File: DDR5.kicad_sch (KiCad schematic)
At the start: 2 parts, among them U12 DDR504111002KQ

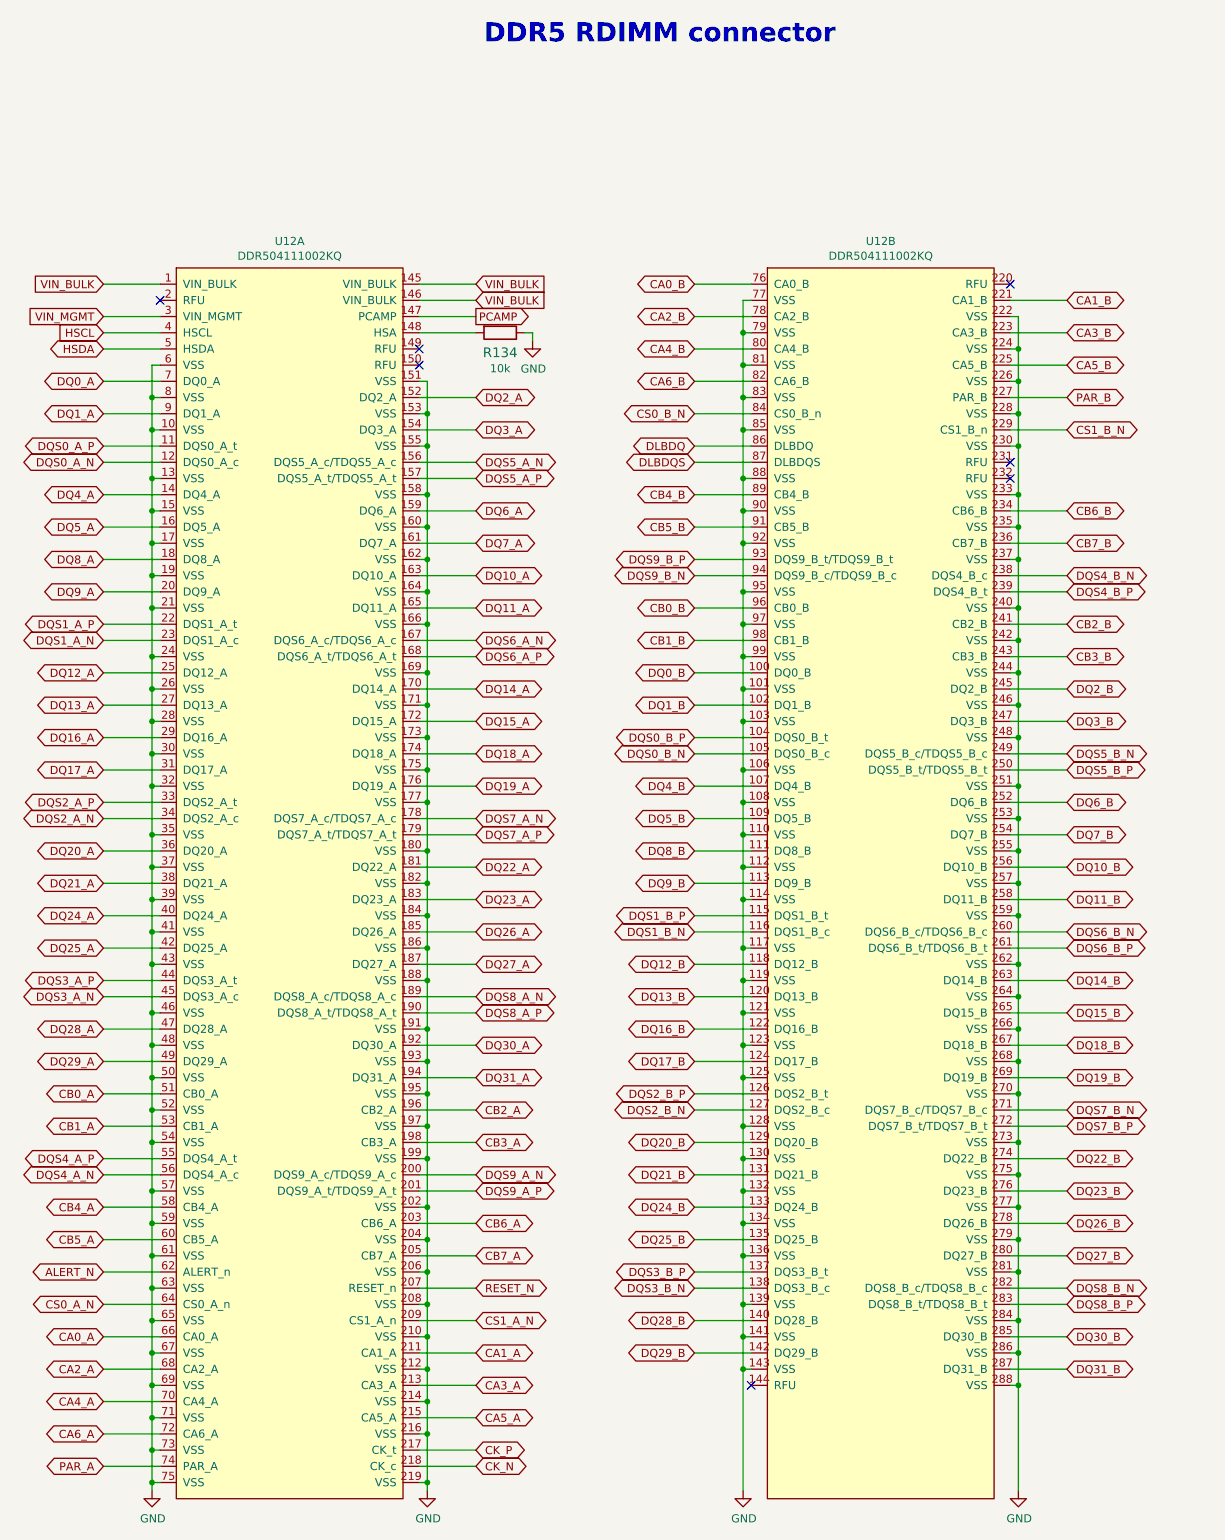
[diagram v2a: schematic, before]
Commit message: Introduce component standarization
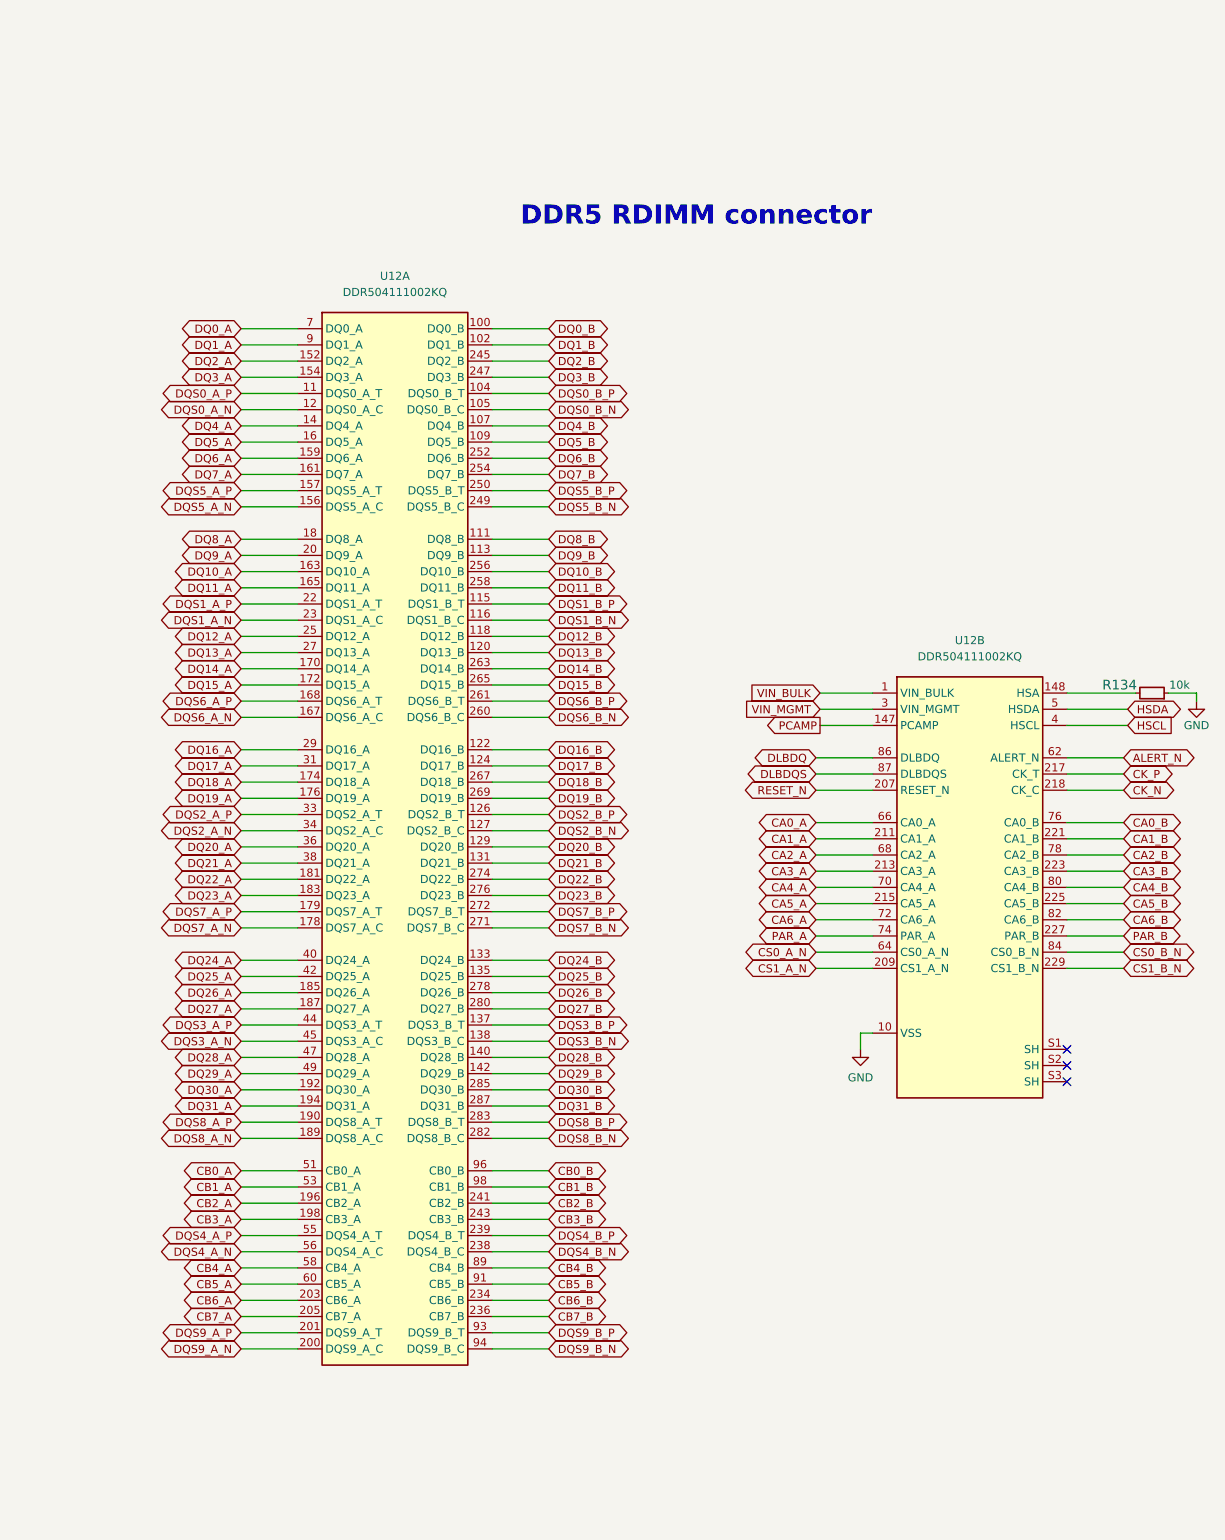
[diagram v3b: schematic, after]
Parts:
- R134: footprint data-center-rdimm-ddr5-tester-footprints:0402-res -> data-center-rdimm-ddr5-tester-footprints:R_0402_1005Metric; Author (none) -> Antmicro; License (none) -> Apache-2.0; MPN CRCW040210K0FKEDHP -> CR0402-FX-1002GLF; Manufacturer VISHAY -> Bourns; Tolerance (none) -> 1%
- U12: value DDR504111002KQ -> Bus_DDR5_DDR504111002KQ; footprint data-center-rdimm-ddr5-tester-footprints:DDR504111002KQ -> data-center-rdimm-ddr5-tester-footprints:Bus_DDR5_Socket_Amphenol_DDR504111002KQ; symbol data-center-rdimm-ddr5-tester:DDR504111002KQ -> data-center-rdimm-ddr5-tester:Bus_DDR5_DDR504111002KQ; Author (none) -> Antmicro; License (none) -> Apache-2.0; Manufacturer (none) -> Amphenol; Manufaturer Amphenol FCI -> (none)
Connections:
- net ALERT_N: now also U12.62 (ALERT_N); no longer U12.62 (ALERT_n)
- net CA0_A: now also U12.66 (CA0_A); no longer U12.66 (CA0_A)
- net CA1_A: now also U12.211 (CA1_A); no longer U12.211 (CA1_A)
- net CA2_A: now also U12.68 (CA2_A); no longer U12.68 (CA2_A)
- net CA3_A: now also U12.213 (CA3_A); no longer U12.213 (CA3_A)
- net CA4_A: now also U12.70 (CA4_A); no longer U12.70 (CA4_A)
- net CA5_A: now also U12.215 (CA5_A); no longer U12.215 (CA5_A)
- net CA6_A: now also U12.72 (CA6_A); no longer U12.72 (CA6_A)
- net CB0_B: now also U12.96 (CB0_B); no longer U12.96 (CB0_B)
- net CB1_B: now also U12.98 (CB1_B); no longer U12.98 (CB1_B)
- net CB2_B: now also U12.241 (CB2_B); no longer U12.241 (CB2_B)
- net CB3_B: now also U12.243 (CB3_B); no longer U12.243 (CB3_B)
- net CB4_B: now also U12.89 (CB4_B); no longer U12.89 (CB4_B)
- net CB5_B: now also U12.91 (CB5_B); no longer U12.91 (CB5_B)
- net CB6_B: now also U12.234 (CB6_B); no longer U12.234 (CB6_B)
- net CB7_B: now also U12.236 (CB7_B); no longer U12.236 (CB7_B)
- net CK_N: now also U12.218 (CK_C); no longer U12.218 (CK_c)
- net CK_P: now also U12.217 (CK_T); no longer U12.217 (CK_t)
- net CS0_A_N: now also U12.64 (CS0_A_N); no longer U12.64 (CS0_A_n)
- net CS1_A_N: now also U12.209 (CS1_A_N); no longer U12.209 (CS1_A_n)
- net DQ0_B: now also U12.100 (DQ0_B); no longer U12.100 (DQ0_B)
- net DQ10_B: now also U12.256 (DQ10_B); no longer U12.256 (DQ10_B)
- net DQ11_B: now also U12.258 (DQ11_B); no longer U12.258 (DQ11_B)
- net DQ12_B: now also U12.118 (DQ12_B); no longer U12.118 (DQ12_B)
- net DQ13_B: now also U12.120 (DQ13_B); no longer U12.120 (DQ13_B)
- net DQ14_B: now also U12.263 (DQ14_B); no longer U12.263 (DQ14_B)
- net DQ15_B: now also U12.265 (DQ15_B); no longer U12.265 (DQ15_B)
- net DQ16_B: now also U12.122 (DQ16_B); no longer U12.122 (DQ16_B)
- net DQ17_B: now also U12.124 (DQ17_B); no longer U12.124 (DQ17_B)
- net DQ18_B: now also U12.267 (DQ18_B); no longer U12.267 (DQ18_B)
- net DQ19_B: now also U12.269 (DQ19_B); no longer U12.269 (DQ19_B)
- net DQ1_B: now also U12.102 (DQ1_B); no longer U12.102 (DQ1_B)
- net DQ20_B: now also U12.129 (DQ20_B); no longer U12.129 (DQ20_B)
- net DQ21_B: now also U12.131 (DQ21_B); no longer U12.131 (DQ21_B)
- net DQ22_B: now also U12.274 (DQ22_B); no longer U12.274 (DQ22_B)
- net DQ23_B: now also U12.276 (DQ23_B); no longer U12.276 (DQ23_B)
- net DQ24_B: now also U12.133 (DQ24_B); no longer U12.133 (DQ24_B)
- net DQ25_B: now also U12.135 (DQ25_B); no longer U12.135 (DQ25_B)
- net DQ26_B: now also U12.278 (DQ26_B); no longer U12.278 (DQ26_B)
- net DQ27_B: now also U12.280 (DQ27_B); no longer U12.280 (DQ27_B)
- net DQ28_B: now also U12.140 (DQ28_B); no longer U12.140 (DQ28_B)
- net DQ29_B: now also U12.142 (DQ29_B); no longer U12.142 (DQ29_B)
- net DQ2_B: now also U12.245 (DQ2_B); no longer U12.245 (DQ2_B)
- net DQ30_B: now also U12.285 (DQ30_B); no longer U12.285 (DQ30_B)
- net DQ31_B: now also U12.287 (DQ31_B); no longer U12.287 (DQ31_B)
- net DQ3_B: now also U12.247 (DQ3_B); no longer U12.247 (DQ3_B)
- net DQ4_B: now also U12.107 (DQ4_B); no longer U12.107 (DQ4_B)
- net DQ5_B: now also U12.109 (DQ5_B); no longer U12.109 (DQ5_B)
- net DQ6_B: now also U12.252 (DQ6_B); no longer U12.252 (DQ6_B)
- net DQ7_B: now also U12.254 (DQ7_B); no longer U12.254 (DQ7_B)
- net DQ8_B: now also U12.111 (DQ8_B); no longer U12.111 (DQ8_B)
- net DQ9_B: now also U12.113 (DQ9_B); no longer U12.113 (DQ9_B)
- net DQS0_B_N: now also U12.105 (DQS0_B_C); no longer U12.105 (DQS0_B_c)
- net DQS0_B_P: now also U12.104 (DQS0_B_T); no longer U12.104 (DQS0_B_t)
- net DQS1_B_N: now also U12.116 (DQS1_B_C); no longer U12.116 (DQS1_B_c)
- net DQS1_B_P: now also U12.115 (DQS1_B_T); no longer U12.115 (DQS1_B_t)
- net DQS2_B_N: now also U12.127 (DQS2_B_C); no longer U12.127 (DQS2_B_c)
- net DQS2_B_P: now also U12.126 (DQS2_B_T); no longer U12.126 (DQS2_B_t)
- net DQS3_B_N: now also U12.138 (DQS3_B_C); no longer U12.138 (DQS3_B_c)
- net DQS3_B_P: now also U12.137 (DQS3_B_T); no longer U12.137 (DQS3_B_t)
- net DQS4_B_N: now also U12.238 (DQS4_B_C); no longer U12.238 (DQS4_B_c)
- net DQS4_B_P: now also U12.239 (DQS4_B_T); no longer U12.239 (DQS4_B_t)
- net DQS5_B_N: now also U12.249 (DQS5_B_C); no longer U12.249 (DQS5_B_c/TDQS5_B_c)
- net DQS5_B_P: now also U12.250 (DQS5_B_T); no longer U12.250 (DQS5_B_t/TDQS5_B_t)
- net DQS6_B_N: now also U12.260 (DQS6_B_C); no longer U12.260 (DQS6_B_c/TDQS6_B_c)
- net DQS6_B_P: now also U12.261 (DQS6_B_T); no longer U12.261 (DQS6_B_t/TDQS6_B_t)
- net DQS7_B_N: now also U12.271 (DQS7_B_C); no longer U12.271 (DQS7_B_c/TDQS7_B_c)
- net DQS7_B_P: now also U12.272 (DQS7_B_T); no longer U12.272 (DQS7_B_t/TDQS7_B_t)
- net DQS8_B_N: now also U12.282 (DQS8_B_C); no longer U12.282 (DQS8_B_c/TDQS8_B_c)
- net DQS8_B_P: now also U12.283 (DQS8_B_T); no longer U12.283 (DQS8_B_t/TDQS8_B_t)
- net DQS9_B_N: now also U12.94 (DQS9_B_C); no longer U12.94 (DQS9_B_c/TDQS9_B_c)
- net DQS9_B_P: now also U12.93 (DQS9_B_T); no longer U12.93 (DQS9_B_t/TDQS9_B_t)
- net GND: now also U12.10 (VSS), U12.13 (VSS), U12.15 (VSS), U12.151 (VSS), U12.153 (VSS), U12.155 (VSS), U12.158 (VSS), U12.160 (VSS), U12.162 (VSS), U12.164 (VSS), U12.166 (VSS), U12.169 (VSS), U12.17 (VSS), U12.171 (VSS), U12.173 (VSS), U12.175 (VSS), U12.177 (VSS), U12.180 (VSS), U12.182 (VSS), U12.184 (VSS), U12.186 (VSS), U12.188 (VSS), U12.19 (VSS), U12.191 (VSS), U12.193 (VSS), U12.195 (VSS), U12.197 (VSS), U12.199 (VSS), U12.202 (VSS), U12.204 (VSS), U12.206 (VSS), U12.208 (VSS), U12.21 (VSS), U12.210 (VSS), U12.212 (VSS), U12.214 (VSS), U12.216 (VSS), U12.219 (VSS), U12.24 (VSS), U12.26 (VSS), U12.28 (VSS), U12.30 (VSS), U12.32 (VSS), U12.35 (VSS), U12.37 (VSS), U12.39 (VSS), U12.41 (VSS), U12.43 (VSS), U12.46 (VSS), U12.48 (VSS), U12.50 (VSS), U12.52 (VSS), U12.54 (VSS), U12.57 (VSS), U12.59 (VSS), U12.6 (VSS), U12.61 (VSS), U12.63 (VSS), U12.65 (VSS), U12.67 (VSS), U12.69 (VSS), U12.71 (VSS), U12.73 (VSS), U12.75 (VSS), U12.8 (VSS); no longer U12.10 (VSS), U12.13 (VSS), U12.15 (VSS), U12.151 (VSS), U12.153 (VSS), U12.155 (VSS), U12.158 (VSS), U12.160 (VSS), U12.162 (VSS), U12.164 (VSS), U12.166 (VSS), U12.169 (VSS), U12.17 (VSS), U12.171 (VSS), U12.173 (VSS), U12.175 (VSS), U12.177 (VSS), U12.180 (VSS), U12.182 (VSS), U12.184 (VSS), U12.186 (VSS), U12.188 (VSS), U12.19 (VSS), U12.191 (VSS), U12.193 (VSS), U12.195 (VSS), U12.197 (VSS), U12.199 (VSS), U12.202 (VSS), U12.204 (VSS), U12.206 (VSS), U12.208 (VSS), U12.21 (VSS), U12.210 (VSS), U12.212 (VSS), U12.214 (VSS), U12.216 (VSS), U12.219 (VSS), U12.24 (VSS), U12.26 (VSS), U12.28 (VSS), U12.30 (VSS), U12.32 (VSS), U12.35 (VSS), U12.37 (VSS), U12.39 (VSS), U12.41 (VSS), U12.43 (VSS), U12.46 (VSS), U12.48 (VSS), U12.50 (VSS), U12.52 (VSS), U12.54 (VSS), U12.57 (VSS), U12.59 (VSS), U12.6 (VSS), U12.61 (VSS), U12.63 (VSS), U12.65 (VSS), U12.67 (VSS), U12.69 (VSS), U12.71 (VSS), U12.73 (VSS), U12.75 (VSS), U12.8 (VSS)
- net HSCL: now also U12.4 (HSCL); no longer U12.4 (HSCL)
- net HSDA: now also U12.5 (HSDA); no longer U12.5 (HSDA)
- net PAR_A: now also U12.74 (PAR_A); no longer U12.74 (PAR_A)
- net PCAMP: now also U12.147 (PCAMP); no longer U12.147 (PCAMP)
- net RESET_N: now also U12.207 (RESET_N); no longer U12.207 (RESET_n)
- net VIN_BULK: now also U12.1 (VIN_BULK), U12.145 (VIN_BULK), U12.146 (VIN_BULK); no longer U12.1 (VIN_BULK), U12.145 (VIN_BULK), U12.146 (VIN_BULK)
- net VIN_MGMT: now also U12.3 (VIN_MGMT); no longer U12.3 (VIN_MGMT)
- net at R134.2: now also U12.148 (HSA); no longer U12.148 (HSA)
- no-connect marks 7 -> 3
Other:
- moved on the sheet: R134
